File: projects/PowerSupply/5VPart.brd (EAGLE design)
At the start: 50 x 50 mm, 26 parts, among them IC1 LM2596T, IC2 LM2596T, X1 IN, X2 OUT

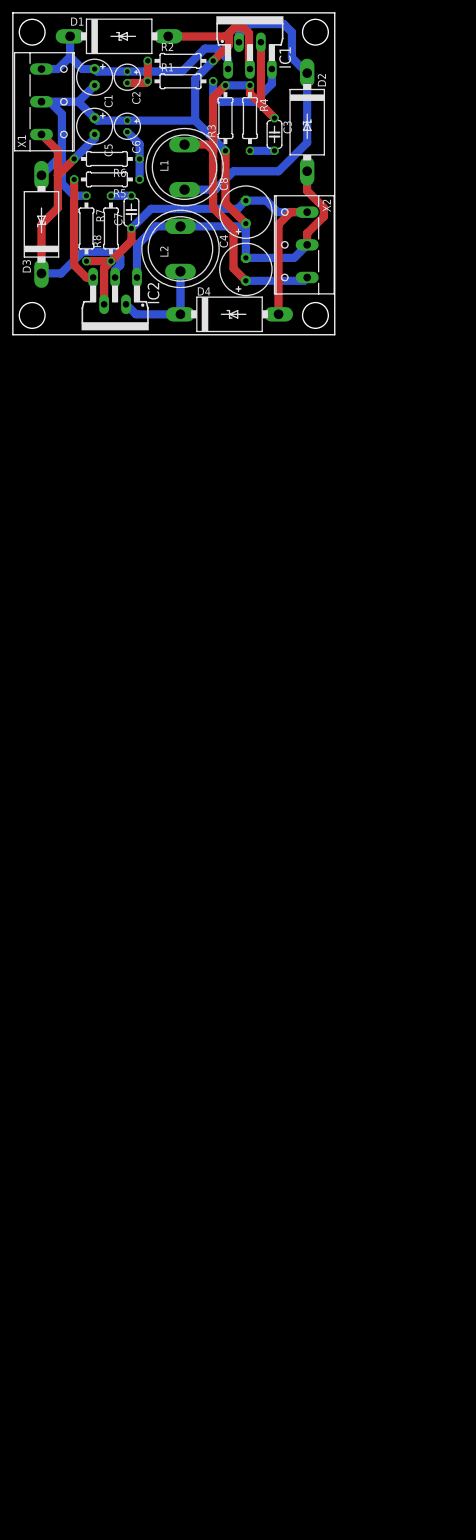
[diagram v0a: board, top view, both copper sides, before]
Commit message: feat: 5 volt part modified
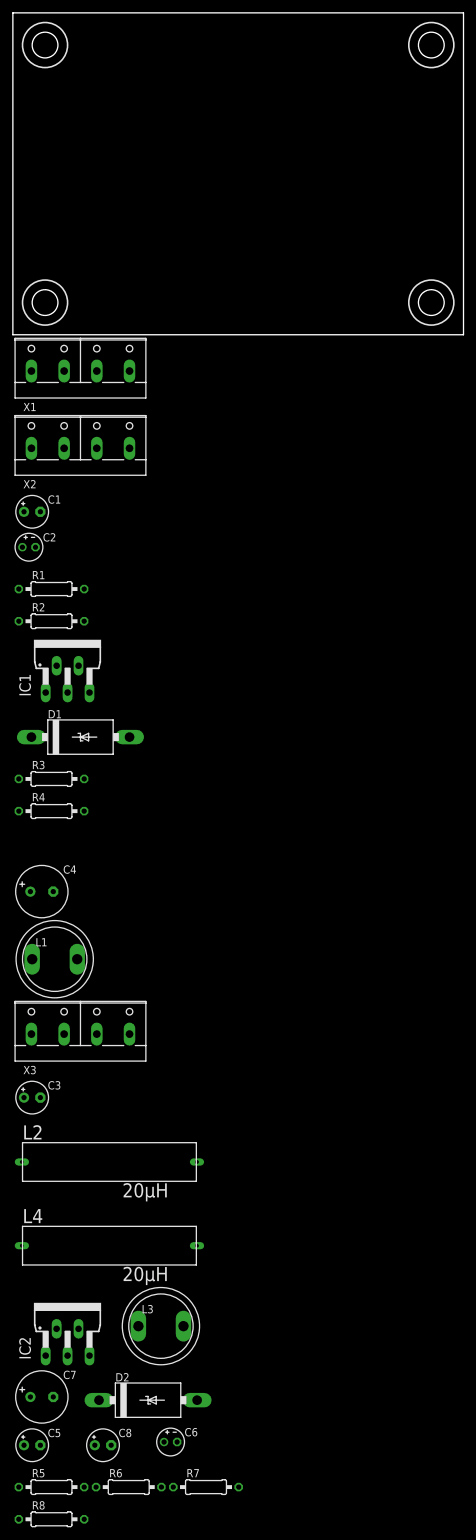
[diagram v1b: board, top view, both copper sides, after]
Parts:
- removed D3, D4: 1N5822, diode:C4111-15
- added L3: 47µH, bb84:IND-120
- added L4: 20µH, bb84:B82111B
- added X3: PWR-OUT, con-wago-508:W237-4P
- C1, C5: device rcl:E2,5-6 -> rcl:E2,5-5
- C2, C6: device rcl:E1,8-4 -> rcl:E2-4
- C3: value 1.2nF -> 100µF; device rcl:C050-024X044 -> rcl:E2,5-5
- C7: value 1.2nF -> 220µF; device rcl:C050-024X044 -> rcl:E3,5-8
- C8: value 470µF -> 100µF; device rcl:E3,5-8 -> rcl:E2,5-5
- L2: value 33µH -> 20µH; device bb84:IND-120 -> bb84:B82111B
- X1: value IN -> PWR-IN; device con-wago-508:W237-133 -> con-wago-508:W237-4P
- X2: value OUT -> CTRL; device con-wago-508:W237-133 -> con-wago-508:W237-4P
- moved R6 206.3 mm to (18.0, -179.0), turned to 0 degrees
- moved C5 205.1 mm to (3.00, -172.5), turned to 0 degrees
- moved C6 204.5 mm to (24.5, -172.0), turned to 0 degrees
- moved R5 203.3 mm to (6.00, -179.0), turned to 0 degrees
- moved R8 200.7 mm to (6.00, -184.0), turned to 0 degrees
- moved D2 200.1 mm to (21.0, -165.5), turned to 0 degrees
- moved R7 196.4 mm to (30.0, -179.0), turned to 0 degrees
- moved C8 192.8 mm to (14.0, -172.5), turned to 0 degrees
- moved C7 184.6 mm to (4.50, -165.0), turned to 0 degrees
- moved IC2 157.5 mm to (8.50, -153.5), turned to 0 degrees
- moved C3 154.3 mm to (3.00, -118.5), turned to 0 degrees
- moved L2 142.3 mm to (15.0, -128.5), turned to 0 degrees
- moved L1 124.7 mm to (6.50, -97.0), turned to 0 degrees
- moved R4 112.0 mm to (6.00, -74.0), turned to 0 degrees
- moved D1 109.0 mm to (10.5, -62.5)
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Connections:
- removed net +20V: C1.+, C2.+, D1.C, IC1.1, X1.1
- removed net +5V: C3.1, C4.+, IC1.4, L1.P$2, R3.2, R4.1, X2.1
- removed net -20V: C5.-, D3.C, IC2.3, R6.2, X1.3
- removed net -5V: C7.1, C8.-, D4.A, IC2.4, R7.2, R8.1, X2.3
- removed net N$3: D2.C, IC1.2, L1.P$1
- new net N$10: IC2.5, R5.2, R6.2
- new net N$11: C5.-, C7.-, D2.A, IC2.3, R6.1, R7.1, X3.4
- new net N$12: D2.C, IC2.2, L3.P$1
- new net N$13: C7.+, L3.P$2, L4.P$1, R8.2
- new net N$14: IC2.4, R7.2, R8.1
- new net N$15: C8.-, L4.P$2
- new net N$9: C6.-, R5.1
- net GND: now also C3.-, R2.1, X1.3, X1.4, X3.2, X3.3; no longer C5.+, C6.+, D2.A, D3.A, IC2.1, L2.P$2, R2.2, R7.1, X1.2, X2.2
- net N$1: now also C1.+, C2.+, C5.+, C6.+, IC1.1, IC2.1, X1.1, X1.2; no longer C3.2, R4.2
- net N$2: now also IC1.5, R1.2, R2.2; no longer D4.C, IC2.2, L2.P$1
- net N$4: now also D1.C, IC1.2, L1.P$1; no longer IC1.5, R1.2
- net N$5: now also IC1.4, R3.2, R4.1; no longer C7.2, R8.2
- net N$6: now also C4.+, L1.P$2, L2.P$1, R4.2; no longer C2.-, R1.1, R2.1
- net N$7: now also C3.+, L2.P$2, X3.1; no longer IC2.5, R5.2
- net N$8: now also C2.-, R1.1; no longer C6.-, R5.1, R6.1
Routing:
- net GND: track 159.3 -> 0.00 mm
- net +5V: track 71.0 -> 0.00 mm
- net -5V: track 66.4 -> 0.00 mm
- net N$3: track 50.8 -> 0.00 mm
- net -20V: track 49.9 -> 0.00 mm
- net +20V: track 37.6 -> 0.00 mm
- net N$7: track 17.1 -> 0.00 mm
- net N$2: track 15.8 -> 0.00 mm
- net N$4: track 15.0 -> 0.00 mm
- net N$8: track 8.16 -> 0.00 mm
- net N$6: track 6.46 -> 0.00 mm
- net N$1: track 3.81 -> 0.00 mm
- net N$5: track 3.17 -> 0.00 mm
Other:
- board size 50 x 50 mm -> 70 x 50 mm

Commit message: feat: 5 volt part modified
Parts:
- removed R7: 1k, rcl:0207/10
- removed R8: 3.09k, rcl:0207/10
- removed X2: CTRL, con-wago-508:W237-4P
- added D3: 1N5822, diode:C4111-15
- added D4: 1N4007, Diodes:DO-41
- C1, C3, C8: device rcl:E2,5-5 -> rcl:E2,5-6
- C2: value 0.1µF -> 220µF; device rcl:E2-4 -> rcl:E2,5-6
- C4: value 220µF -> 100µF; device rcl:E3,5-8 -> rcl:E2,5-6
- C5: value 100µF -> 0.1µF; device rcl:E2,5-5 -> rcl:E2-4
- C6: value 0.1µF -> 1000µF; device rcl:E2-4 -> rcl:E5-10,5
- C7: value 220µF -> 1000µF; device rcl:E3,5-8 -> rcl:E5-10,5
- D2: value 1N5822 -> 1N4007; device diode:C4111-15 -> Diodes:DO-41
- L3: value 47µH -> 33µH
- R1, R5: value 47k -> 1k
- R2, R6: value 47k -> 3.09k
- R3: value 1k -> 47k
- R4: value 3.09k -> 47k
- moved C2 201.6 mm to (-1.27, -234.6)
- moved C1 194.4 mm to (-1.27, -221.9)
- moved D2 130.9 mm to (-1.50, -294.5)
- moved C3 128.9 mm to (-1.27, -247.3)
- moved C4 122.8 mm to (-1.27, -209.2)
- moved C6 116.6 mm to (-2.54, -285.4)
- moved R3 110.0 mm to (6.00, -179.0)
- moved C7 107.9 mm to (-2.54, -272.7)
- moved R4 105.7 mm to (18.0, -179.0)
- moved C8 88.8 mm to (-1.27, -260.0)
- moved R1 29.5 mm to (6.00, -69.0)
- moved R2 29.5 mm to (6.00, -74.0)
- moved R5 24.0 mm to (30.0, -179.0)
- moved C5 21.5 mm to (24.5, -172.0)
- moved R6 13.0 mm to (6.00, -184.0)
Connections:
- removed net N$13: C7.+, L3.P$2, L4.P$1, R8.2
- removed net N$15: C8.-, L4.P$2
- removed net N$2: IC1.5, R1.2, R2.2
- removed net N$8: C2.-, R1.1
- new net N$3: C8.-, D4.A, L4.P$2, X3.4
- new net VCC: C1.+, D2.A, IC1.1, X1.1, X1.2
- net GND: now also C2.-, C6.+, C7.+, D4.C, IC1.5, L3.P$2, R1.1, R6.2; no longer R2.1, R3.1
- net N$1: now also C4.+, D2.C; no longer C1.+, C2.+, C6.+, IC1.1, X1.1, X1.2
- net N$10: now also R3.2, R4.2; no longer R5.2, R6.2
- net N$11: now also C6.-, D3.A, L4.P$1, R4.1, R5.1; no longer C5.-, D2.A, R6.1, R7.1, X3.4
- net N$12: now also D3.C; no longer D2.C
- net N$14: now also R5.2, R6.1; no longer R7.2, R8.1
- net N$5: now also R1.2, R2.1; no longer R3.2, R4.1
- net N$6: now also C2.+, R2.2; no longer C4.+, R4.2
- net N$9: now also C5.-, R3.1; no longer C6.-, R5.1

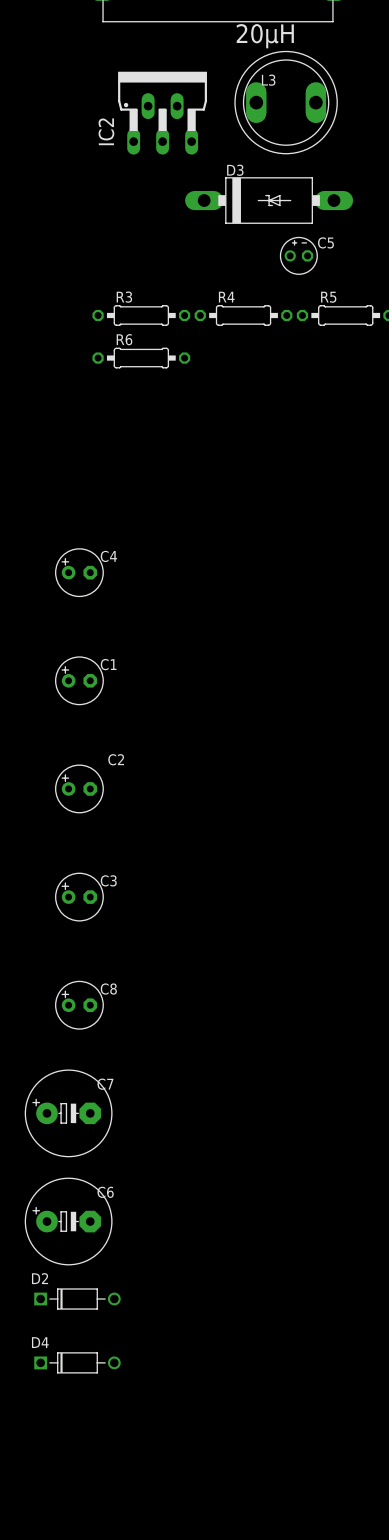
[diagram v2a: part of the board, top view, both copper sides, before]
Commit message: feat: 5 volt part modified
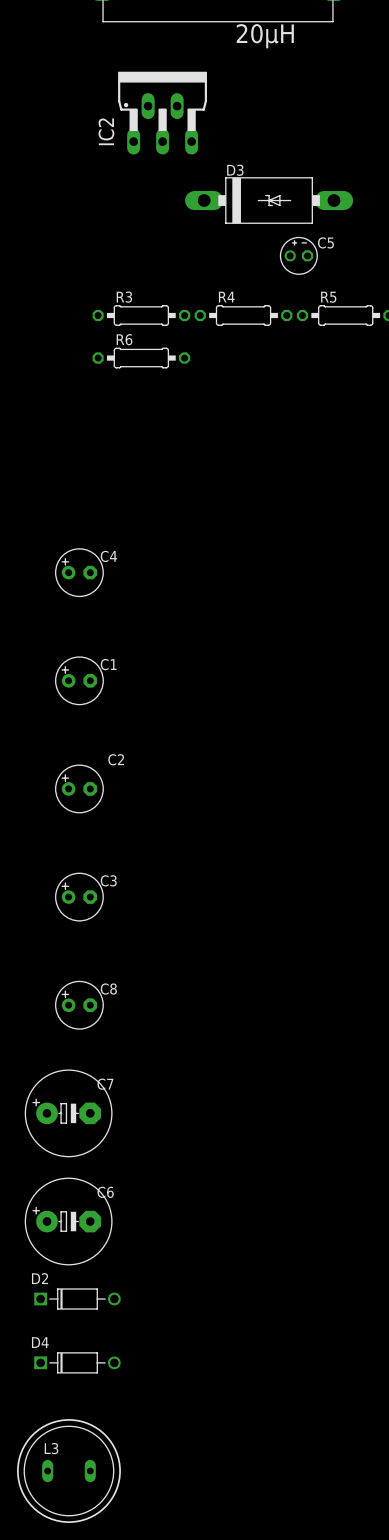
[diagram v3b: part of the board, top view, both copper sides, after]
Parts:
- L3: value 33µH -> 220µH; device bb84:IND-120 -> bb84:11PHC
- moved L3 162.7 mm to (-2.50, -314.7)
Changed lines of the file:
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@@
 <attribute name="VALUE" x="-4.826" y="-288.448" size="1.27" layer="27" ratio="10"/>
 </element>
-<element name="L3" library="bb84" package="IND-120" value="33µH" x="23" y="-154" smashed="yes">
-<attribute name="NAME" x="20" y="-152" size="1.27" layer="25"/>
-<attribute name="VALUE" x="20" y="-157" size="1.27" layer="27"/>
+<element name="L3" library="bb84" package="11PHC" value="220µH" x="-2.5" y="-314.7" smashed="yes">
+<attribute name="NAME" x="-5.5" y="-312.7" size="1.27" layer="25"/>
+<attribute name="VALUE" x="-5.5" y="-317.7" size="1.27" layer="27"/>
 </element>
 <element name="L4" library="bb84" package="B82111B" value="20µH" x="15" y="-141.5" smashed="yes">
@@
 <wire x1="-5.08" y1="-285.4" x2="-5.08" y2="-272.7" width="0" layer="19" extent="1-1"/>
 <wire x1="-5.825" y1="-302" x2="-5.08" y2="-285.4" width="0" layer="19" extent="1-1"/>
+<wire x1="0" y1="-314.7" x2="-5.825" y2="-302" width="0" layer="19" extent="1-1"/>
 <wire x1="11.08" y1="-184" x2="0" y2="-209.2" width="0" layer="19" extent="1-1"/>
-<wire x1="26.5" y1="-154" x2="11.08" y2="-184" width="0" layer="19" extent="1-1"/>
-<wire x1="13.04" y1="-108.635" x2="26.5" y2="-154" width="0" layer="19" extent="1-1"/>
+<wire x1="13.04" y1="-108.635" x2="11.08" y2="-184" width="0" layer="19" extent="1-1"/>
 <wire x1="7.96" y1="-108.635" x2="13.04" y2="-108.635" width="0" layer="19" extent="1-1"/>
 <wire x1="0.92" y1="-69" x2="7.96" y2="-108.635" width="0" layer="19" extent="1-1"/>
@@
 <contactref element="D3" pad="C"/>
 <wire x1="6.7982" y1="-154.4144" x2="13.38" y2="-165.5" width="0" layer="19" extent="1-1"/>
-<wire x1="19.5" y1="-154" x2="6.7982" y2="-154.4144" width="0" layer="19" extent="1-1"/>
+<wire x1="-5" y1="-314.7" x2="13.38" y2="-165.5" width="0" layer="19" extent="1-1"/>
 </signal>
 <signal name="N$14">

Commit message: feat: 5 volt part modified
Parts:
- removed X3: PWR-OUT, con-wago-508:W237-4P
- added X2: PWR-OUT, con-wago-508:W237-133
- moved D4 370.4 mm to (25.0, 67.5)
- moved L3 360.6 mm to (43.0, 43.0)
- moved C6 342.6 mm to (40.0, 54.5), turned to 180 degrees
- moved C7 340.3 mm to (43.5, 64.5), turned to 180 degrees
- moved C8 328.3 mm to (33.5, 66.5)
- moved D2 306.6 mm to (25.0, 11.0), turned to 180 degrees
- moved C3 287.7 mm to (22.0, 39.5), turned to 180 degrees
- moved C2 274.6 mm to (16.0, 39.5)
- moved R6 241.2 mm to (48.0, 53.5), turned to 270 degrees
- moved C1 236.0 mm to (7.00, 14.0)
- moved R5 232.5 mm to (33.0, 53.5), turned to 90 degrees
- moved C4 227.4 mm to (36.5, 15.0), flipped to the bottom
- moved R4 215.5 mm to (43.0, 35.0)
- moved L4 203.5 mm to (16.0, 62.0)
- moved R3 200.9 mm to (48.0, 17.5), turned to 90 degrees
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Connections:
- net GND: now also X2.2; no longer X3.2, X3.3
- net N$3: now also X2.1; no longer X3.4
- net N$7: now also X2.3; no longer X3.1
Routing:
- net GND: track 0.00 -> 183.1 mm
- net N$11: track 0.00 -> 107.2 mm
- net N$14: track 0.00 -> 51.5 mm
- net N$7: track 0.00 -> 49.4 mm
- net N$12: track 0.00 -> 38.2 mm
- net VCC: track 0.00 -> 35.4 mm
- net N$6: track 0.00 -> 33.9 mm
- net N$4: track 0.00 -> 30.3 mm
- net N$5: track 0.00 -> 26.1 mm
- net N$3: track 0.00 -> 25.9 mm
- net N$1: track 0.00 -> 21.0 mm
- net N$10: track 0.00 -> 16.7 mm
- net N$9: track 0.00 -> 6.87 mm
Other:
- board size 70 x 50 mm -> 50 x 80 mm
